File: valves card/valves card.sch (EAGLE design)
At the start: 68 parts, among them J1 TBP02R1-381-14BE, J2 09231486921, M1 SAM_D21_MINI_BREAKOUT, T1 IRLZ44NSTRLPBF, T10 IRLZ44NSTRLPBF, T11 IRLZ44NSTRLPBF, T12 IRLZ44NSTRLPBF, T2 IRLZ44NSTRLPBF, T3 IRLZ44NSTRLPBF, T4 IRLZ44NSTRLPBF, T5 IRLZ44NSTRLPBF, T6 IRLZ44NSTRLPBF, T7 IRLZ44NSTRLPBF, T8 IRLZ44NSTRLPBF, T9 IRLZ44NSTRLPBF, U1 LM2937IMP-12, U10 EL817(D)-ND, U11 EL817(D)-ND, U12 EL817(D)-ND, U13 EL817(D)-ND, U2 EL817(D)-ND, U3 EL817(D)-ND, U4 EL817(D)-ND, U5 EL817(D)-ND, U6 EL817(D)-ND, U7 EL817(D)-ND, U8 EL817(D)-ND, U9 EL817(D)-ND

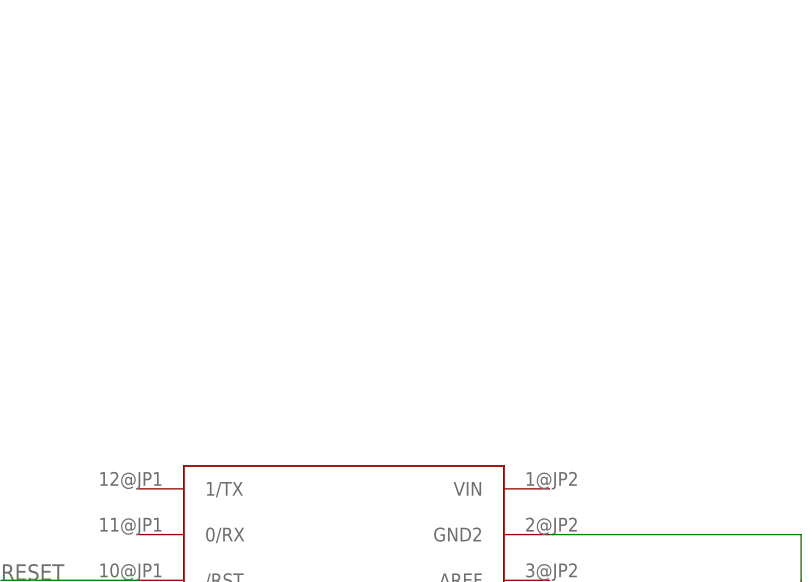
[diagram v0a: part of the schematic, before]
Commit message: made card holes bigger, started usb port work, but I'm not done that part yet
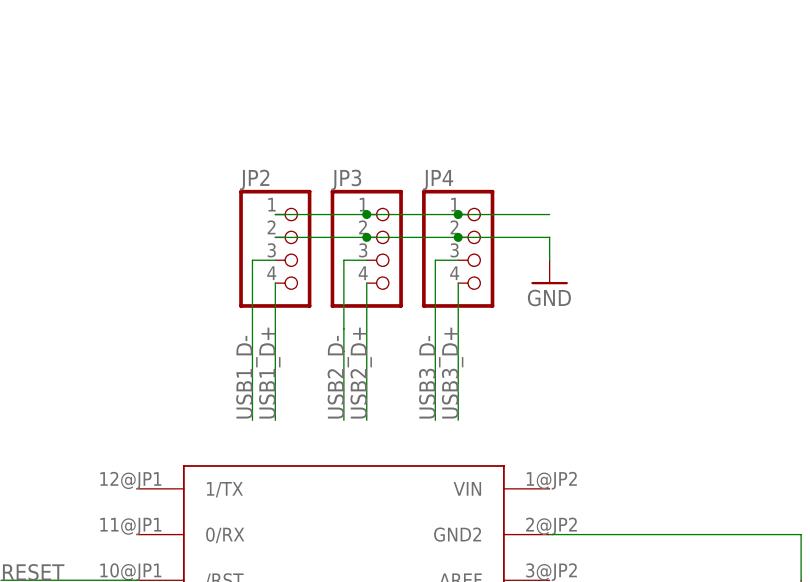
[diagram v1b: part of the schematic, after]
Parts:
- added JP2, JP3, JP4: (no value), pinhead:PINHD-1X4
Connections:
- net 5V: now also JP2.1, JP3.1, JP4.1
- net GND: now also JP2.2, JP3.2, JP4.2
- net USB1_D+: now also JP2.4
- net USB1_D-: now also JP2.3
- net USB2_D+: now also JP3.4
- net USB2_D-: now also JP3.3
- net USB3_D+: now also JP4.4
- net USB3_D-: now also JP4.3
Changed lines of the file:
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@@
 <part name="GND2" library="supply1" library_urn="urn:adsk.eagle:library:371" deviceset="GND" device=""/>
 <part name="GND3" library="supply1" library_urn="urn:adsk.eagle:library:371" deviceset="GND" device=""/>
+<part name="JP2" library="pinhead" library_urn="urn:adsk.eagle:library:325" deviceset="PINHD-1X4" device="" package3d_urn="urn:adsk.eagle:package:22407/2"/>
+<part name="JP3" library="pinhead" library_urn="urn:adsk.eagle:library:325" deviceset="PINHD-1X4" device="" package3d_urn="urn:adsk.eagle:package:22407/2"/>
+<part name="JP4" library="pinhead" library_urn="urn:adsk.eagle:library:325" deviceset="PINHD-1X4" device="" package3d_urn="urn:adsk.eagle:package:22407/2"/>
+<part name="GND7" library="supply1" library_urn="urn:adsk.eagle:library:371" deviceset="GND" device=""/>
 </parts>
 <sheets>
@@
 <attribute name="VALUE" x="-5.08" y="38.1" size="1.778" layer="96"/>
 </instance>
+<instance part="JP2" gate="A" x="71.12" y="93.98" smashed="yes">
+<attribute name="NAME" x="64.77" y="102.235" size="1.778" layer="95"/>
+<attribute name="VALUE" x="64.77" y="86.36" size="1.778" layer="96"/>
+</instance>
+<instance part="JP3" gate="A" x="81.28" y="93.98" smashed="yes">
+<attribute name="NAME" x="74.93" y="102.235" size="1.778" layer="95"/>
+<attribute name="VALUE" x="74.93" y="86.36" size="1.778" layer="96"/>
+</instance>
+<instance part="JP4" gate="A" x="91.44" y="93.98" smashed="yes">
+<attribute name="NAME" x="85.09" y="102.235" size="1.778" layer="95"/>
+<attribute name="VALUE" x="85.09" y="86.36" size="1.778" layer="96"/>
+</instance>
+<instance part="GND7" gate="1" x="99.06" y="91.44" smashed="yes">
+<attribute name="VALUE" x="96.52" y="88.9" size="1.778" layer="96"/>
+</instance>
 </instances>
 <busses>
@@
 <pinref part="J2" gate="G$1" pin="19"/>
 </segment>
+<segment>
+<pinref part="JP2" gate="A" pin="2"/>
+<pinref part="JP3" gate="A" pin="2"/>
+<wire x1="68.58" y1="96.52" x2="78.74" y2="96.52" width="0.1524" layer="91"/>
+<pinref part="JP4" gate="A" pin="2"/>
+<wire x1="78.74" y1="96.52" x2="88.9" y2="96.52" width="0.1524" layer="91"/>
+<junction x="78.74" y="96.52"/>
+<wire x1="88.9" y1="96.52" x2="99.06" y2="96.52" width="0.1524" layer="91"/>
+<junction x="88.9" y="96.52"/>
+<wire x1="99.06" y1="96.52" x2="99.06" y2="93.98" width="0.1524" layer="91"/>
+<pinref part="GND7" gate="1" pin="GND"/>
+</segment>
 </net>
 <net name="24V/12V" class="0">
@@
 <pinref part="J2" gate="G$1" pin="16"/>
 </segment>
+<segment>
+<pinref part="JP2" gate="A" pin="4"/>
+<wire x1="68.58" y1="91.44" x2="68.58" y2="76.2" width="0.1524" layer="91"/>
+<label x="68.58" y="76.2" size="1.778" layer="95" rot="R90"/>
+</segment>
 </net>
 <net name="CS_8" class="0">
@@
 <label x="0" y="48.26" size="1.778" layer="95"/>
 <pinref part="J2" gate="G$1" pin="32"/>
+</segment>
+<segment>
+<pinref part="JP3" gate="A" pin="4"/>
+<wire x1="78.74" y1="91.44" x2="78.74" y2="76.2" width="0.1524" layer="91"/>
+<label x="78.74" y="76.2" size="1.778" layer="95" rot="R90"/>
 </segment>
 </net>
@@
 <pinref part="J2" gate="G$1" pin="39"/>
 </segment>
+<segment>
+<pinref part="JP2" gate="A" pin="1"/>
+<pinref part="JP3" gate="A" pin="1"/>
+<wire x1="68.58" y1="99.06" x2="78.74" y2="99.06" width="0.1524" layer="91"/>
+<pinref part="JP4" gate="A" pin="1"/>
+<wire x1="78.74" y1="99.06" x2="88.9" y2="99.06" width="0.1524" layer="91"/>
+<junction x="78.74" y="99.06"/>
+<wire x1="88.9" y1="99.06" x2="99.06" y2="99.06" width="0.1524" layer="91"/>
+<junction x="88.9" y="99.06"/>
+</segment>
 </net>
 <net name="SDA" class="0">
@@
 <pinref part="J2" gate="G$1" pin="46"/>
 </segment>
+<segment>
+<pinref part="JP4" gate="A" pin="3"/>
+<wire x1="88.9" y1="93.98" x2="86.36" y2="93.98" width="0.1524" layer="91"/>
+<wire x1="86.36" y1="93.98" x2="86.36" y2="76.2" width="0.1524" layer="91"/>
+<label x="86.36" y="76.2" size="1.778" layer="95" rot="R90"/>
+</segment>
 </net>
 <net name="RESET" class="0">
@@
 <pinref part="J2" gate="G$1" pin="15"/>
 </segment>
+<segment>
+<pinref part="JP2" gate="A" pin="3"/>
+<wire x1="68.58" y1="93.98" x2="66.04" y2="93.98" width="0.1524" layer="91"/>
+<wire x1="66.04" y1="93.98" x2="66.04" y2="76.2" width="0.1524" layer="91"/>
+<label x="66.04" y="76.2" size="1.778" layer="95" rot="R90"/>
+</segment>
 </net>
 <net name="CS_6" class="0">
@@
 <pinref part="J2" gate="G$1" pin="31"/>
 </segment>
+<segment>
+<pinref part="JP3" gate="A" pin="3"/>
+<wire x1="78.74" y1="93.98" x2="76.2" y2="93.98" width="0.1524" layer="91"/>
+<wire x1="76.2" y1="93.98" x2="76.2" y2="86.36" width="0.1524" layer="91"/>
+<label x="76.2" y="76.2" size="1.778" layer="95" rot="R90"/>
+<wire x1="76.2" y1="86.36" x2="76.2" y2="83.82" width="0.1524" layer="91"/>
+<wire x1="76.2" y1="83.82" x2="76.2" y2="76.2" width="0.1524" layer="91"/>
+</segment>
 </net>
 <net name="CS_13" class="0">
@@
 <pinref part="J2" gate="G$1" pin="47"/>
 </segment>
-</net>
+<segment>
+<pinref part="JP4" gate="A" pin="4"/>
+<wire x1="88.9" y1="91.44" x2="88.9" y2="76.2" width="0.1524" layer="91"/>
+<label x="88.9" y="76.2" size="1.778" layer="95" rot="R90"/>
+</segment>
+</net>

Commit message: USB system mods complete on the main board, valves board, and motor board
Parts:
- renumbered M1 to M2
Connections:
- new net N$1: M2.GND
- net GND: no longer M2.GND
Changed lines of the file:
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@@
 <part name="GND13" library="supply1" library_urn="urn:adsk.eagle:library:371" deviceset="GND" device=""/>
 <part name="GND14" library="supply1" library_urn="urn:adsk.eagle:library:371" deviceset="GND" device=""/>
-<part name="M1" library="SparkFun-SAMD21-Mini-Breakout" deviceset="SAM_D21_MINI_BREAKOUT" device=""/>
 <part name="T1" library="BUK9214-30A,118" deviceset="BUK9214-30A-118" device="-DPAK" package3d_urn="urn:adsk.eagle:package:30824558/1" value="IRLZ44NSTRLPBF"/>
 <part name="J1" library="TBP02R1-381-14BE" deviceset="TBP02R1-381-14BE" device=""/>
@@
 <part name="JP4" library="pinhead" library_urn="urn:adsk.eagle:library:325" deviceset="PINHD-1X4" device="" package3d_urn="urn:adsk.eagle:package:22407/2"/>
 <part name="GND7" library="supply1" library_urn="urn:adsk.eagle:library:371" deviceset="GND" device=""/>
+<part name="M2" library="SparkFun-SAMD21-Mini-Breakout" deviceset="SAM_D21_MINI_BREAKOUT" device=""/>
 </parts>
 <sheets>
@@
 <attribute name="VALUE" x="259.08" y="-20.32" size="1.778" layer="96"/>
 </instance>
-<instance part="M1" gate="G$1" x="76.2" y="35.56" smashed="yes"/>
 <instance part="T1" gate="T" x="254" y="55.88" smashed="yes">
 <attribute name="NAME" x="251.46" y="56.642" size="1.778" layer="95" rot="R90"/>
@@
 <attribute name="VALUE" x="96.52" y="88.9" size="1.778" layer="96"/>
 </instance>
+<instance part="M2" gate="G$1" x="76.2" y="35.56" smashed="yes"/>
 </instances>
 <busses>
@@
 </segment>
 <segment>
-<pinref part="M1" gate="G$1" pin="GND2"/>
 <wire x1="99.06" y1="63.5" x2="127" y2="63.5" width="0.1524" layer="91"/>
 <wire x1="127" y1="63.5" x2="127" y2="58.42" width="0.1524" layer="91"/>
 <pinref part="GND4" gate="1" pin="GND"/>
-</segment>
-<segment>
-<pinref part="M1" gate="G$1" pin="GND"/>
-<wire x1="53.34" y1="53.34" x2="35.56" y2="53.34" width="0.1524" layer="91"/>
-<wire x1="35.56" y1="53.34" x2="35.56" y2="50.8" width="0.1524" layer="91"/>
-<pinref part="GND5" gate="1" pin="GND"/>
+<pinref part="M2" gate="G$1" pin="GND2"/>
 </segment>
 <segment>
@@
 <net name="3.3V" class="0">
 <segment>
-<pinref part="M1" gate="G$1" pin="VCC"/>
 <wire x1="99.06" y1="53.34" x2="121.92" y2="53.34" width="0.1524" layer="91"/>
 <label x="109.22" y="53.34" size="1.778" layer="95"/>
+<pinref part="M2" gate="G$1" pin="VCC"/>
 </segment>
 <segment>
@@
 <net name="SCK" class="0">
 <segment>
-<pinref part="M1" gate="G$1" pin="13"/>
 <wire x1="99.06" y1="27.94" x2="121.92" y2="27.94" width="0.1524" layer="91"/>
 <label x="109.22" y="27.94" size="1.778" layer="95"/>
+<pinref part="M2" gate="G$1" pin="13"/>
 </segment>
 <segment>
@@
 <net name="MISO" class="0">
 <segment>
-<pinref part="M1" gate="G$1" pin="12"/>
 <wire x1="99.06" y1="22.86" x2="121.92" y2="22.86" width="0.1524" layer="91"/>
 <label x="109.22" y="22.86" size="1.778" layer="95"/>
+<pinref part="M2" gate="G$1" pin="12"/>
 </segment>
 <segment>
@@
 <net name="MOSI" class="0">
 <segment>
-<pinref part="M1" gate="G$1" pin="11"/>
 <wire x1="99.06" y1="17.78" x2="121.92" y2="17.78" width="0.1524" layer="91"/>
 <label x="109.22" y="17.78" size="1.778" layer="95"/>
+<pinref part="M2" gate="G$1" pin="11"/>
 </segment>
 <segment>
@@
 </segment>
 <segment>
-<pinref part="M1" gate="G$1" pin="2"/>
 <wire x1="53.34" y1="48.26" x2="40.64" y2="48.26" width="0.1524" layer="91"/>
 <label x="40.64" y="48.26" size="1.778" layer="95"/>
+<pinref part="M2" gate="G$1" pin="2"/>
 </segment>
 </net>
@@
 </segment>
 <segment>
-<pinref part="M1" gate="G$1" pin="3"/>
 <wire x1="53.34" y1="43.18" x2="40.64" y2="43.18" width="0.1524" layer="91"/>
 <label x="40.64" y="43.18" size="1.778" layer="95"/>
+<pinref part="M2" gate="G$1" pin="3"/>
 </segment>
 </net>
@@
 </segment>
 <segment>
-<pinref part="M1" gate="G$1" pin="4"/>
 <wire x1="53.34" y1="38.1" x2="40.64" y2="38.1" width="0.1524" layer="91"/>
 <label x="40.64" y="38.1" size="1.778" layer="95"/>
+<pinref part="M2" gate="G$1" pin="4"/>
 </segment>
 </net>
@@
 </segment>
 <segment>
-<pinref part="M1" gate="G$1" pin="5"/>
 <wire x1="53.34" y1="33.02" x2="40.64" y2="33.02" width="0.1524" layer="91"/>
 <label x="40.64" y="33.02" size="1.778" layer="95"/>
+<pinref part="M2" gate="G$1" pin="5"/>
 </segment>
 </net>
@@
 </segment>
 <segment>
-<pinref part="M1" gate="G$1" pin="6"/>
 <wire x1="53.34" y1="27.94" x2="40.64" y2="27.94" width="0.1524" layer="91"/>
 <label x="40.64" y="27.94" size="1.778" layer="95"/>
+<pinref part="M2" gate="G$1" pin="6"/>
 </segment>
 </net>
@@
 </segment>
 <segment>
-<pinref part="M1" gate="G$1" pin="7"/>
 <wire x1="53.34" y1="22.86" x2="38.1" y2="22.86" width="0.1524" layer="91"/>
 <label x="40.64" y="22.86" size="1.778" layer="95"/>
+<pinref part="M2" gate="G$1" pin="7"/>
 </segment>
 </net>
@@
 </segment>
 <segment>
-<pinref part="M1" gate="G$1" pin="8"/>
 <wire x1="53.34" y1="17.78" x2="38.1" y2="17.78" width="0.1524" layer="91"/>
 <label x="40.64" y="17.78" size="1.778" layer="95"/>
+<pinref part="M2" gate="G$1" pin="8"/>
 </segment>
 </net>
@@
 </segment>
 <segment>
-<pinref part="M1" gate="G$1" pin="9"/>
 <wire x1="53.34" y1="12.7" x2="38.1" y2="12.7" width="0.1524" layer="91"/>
 <label x="40.64" y="12.7" size="1.778" layer="95"/>
+<pinref part="M2" gate="G$1" pin="9"/>
 </segment>
 </net>
@@
 </segment>
 <segment>
-<pinref part="M1" gate="G$1" pin="A0"/>
 <wire x1="99.06" y1="33.02" x2="121.92" y2="33.02" width="0.1524" layer="91"/>
 <label x="109.22" y="33.02" size="1.778" layer="95"/>
+<pinref part="M2" gate="G$1" pin="A0"/>
 </segment>
 </net>
@@
 </segment>
 <segment>
-<pinref part="M1" gate="G$1" pin="A1"/>
 <wire x1="121.92" y1="38.1" x2="99.06" y2="38.1" width="0.1524" layer="91"/>
 <label x="109.22" y="38.1" size="1.778" layer="95"/>
+<pinref part="M2" gate="G$1" pin="A1"/>
 </segment>
 </net>
@@
 </segment>
 <segment>
-<pinref part="M1" gate="G$1" pin="A2"/>
 <wire x1="99.06" y1="43.18" x2="121.92" y2="43.18" width="0.1524" layer="91"/>
 <label x="109.22" y="43.18" size="1.778" layer="95"/>
+<pinref part="M2" gate="G$1" pin="A2"/>
 </segment>
 </net>
@@
 </segment>
 <segment>
-<pinref part="M1" gate="G$1" pin="A3"/>
 <wire x1="121.92" y1="48.26" x2="99.06" y2="48.26" width="0.1524" layer="91"/>
 <label x="109.22" y="48.26" size="1.778" layer="95"/>
+<pinref part="M2" gate="G$1" pin="A3"/>
 </segment>
 </net>
@@
 <segment>
 <pinref part="SJ1" gate="1" pin="1"/>
-<pinref part="M1" gate="G$1" pin="10"/>
 <wire x1="132.08" y1="12.7" x2="129.54" y2="12.7" width="0.1524" layer="91"/>
 <pinref part="JP1" gate="G$1" pin="1"/>
@@
 <wire x1="129.54" y1="20.32" x2="129.54" y2="12.7" width="0.1524" layer="91"/>
 <junction x="129.54" y="12.7"/>
+<pinref part="M2" gate="G$1" pin="10"/>
 </segment>
 </net>
@@
 </segment>
 <segment>
-<pinref part="M1" gate="G$1" pin="/RST"/>
 <wire x1="53.34" y1="58.42" x2="38.1" y2="58.42" width="0.1524" layer="91"/>
 <label x="38.1" y="58.42" size="1.778" layer="95"/>
+<pinref part="M2" gate="G$1" pin="/RST"/>
 </segment>
 </net>
@@
 </segment>
 </net>
+<net name="N$1" class="0">
+<segment>
+<wire x1="53.34" y1="53.34" x2="35.56" y2="53.34" width="0.1524" layer="91"/>
+<wire x1="35.56" y1="53.34" x2="35.56" y2="50.8" width="0.1524" layer="91"/>
+<pinref part="GND5" gate="1" pin="GND"/>
+<pinref part="M2" gate="G$1" pin="GND"/>
+</segment>
+</net>

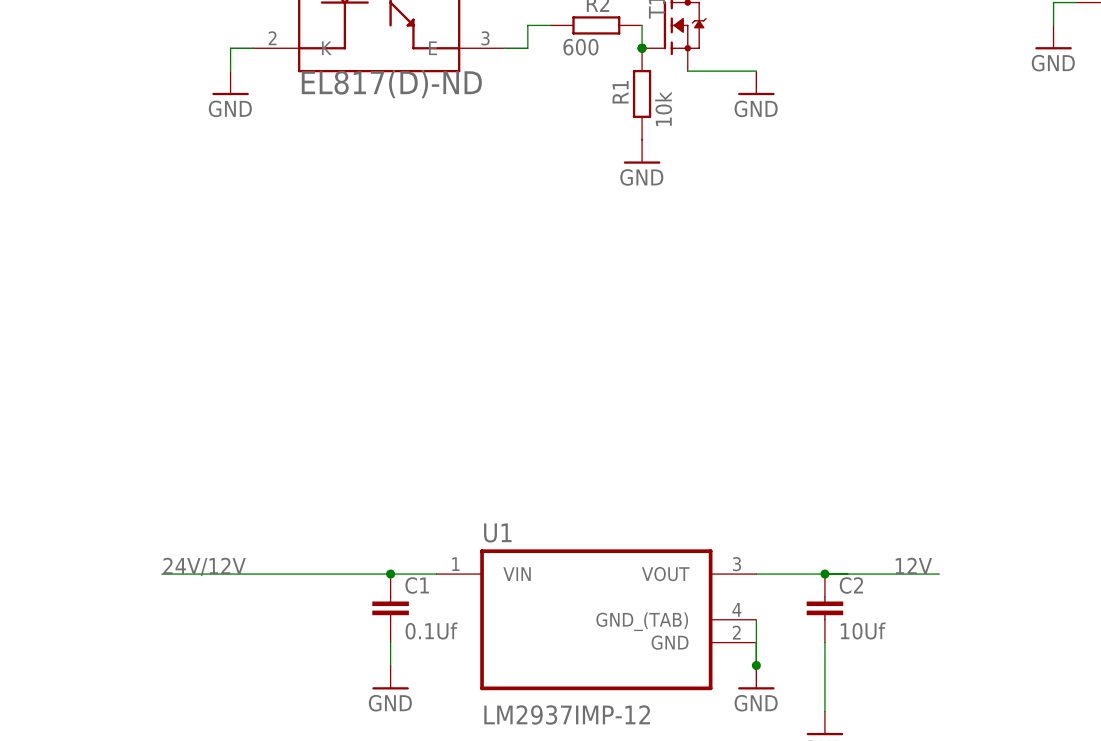
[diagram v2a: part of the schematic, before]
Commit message: added on light to main card
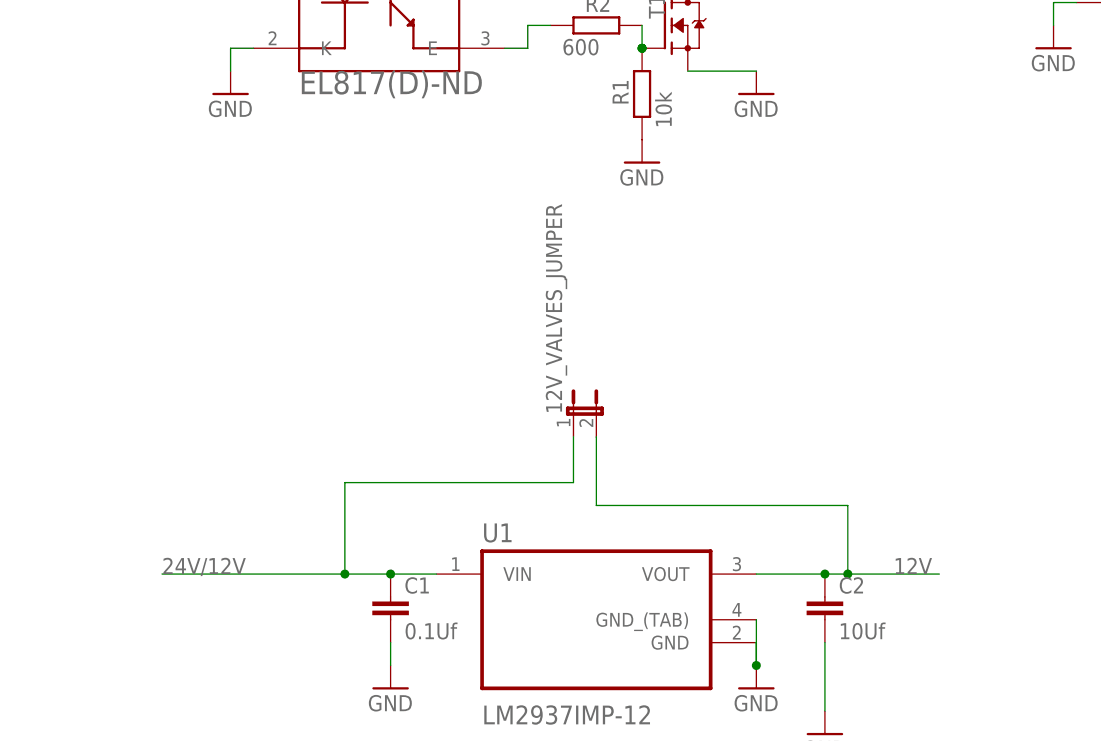
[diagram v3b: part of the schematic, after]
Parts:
- added 12V_VALVES_JUMPER: (no value), SparkFun-Passives:JUMPER-2SMD-NO
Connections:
- net 12V: now also 12V_VALVES_JUMPER.2
- net 24V/12V: now also 12V_VALVES_JUMPER.1
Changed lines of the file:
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@@
 <part name="GND7" library="supply1" library_urn="urn:adsk.eagle:library:371" deviceset="GND" device=""/>
 <part name="M2" library="SparkFun-SAMD21-Mini-Breakout" deviceset="SAM_D21_MINI_BREAKOUT" device=""/>
+<part name="12V_VALVES_JUMPER" library="SparkFun-Passives" deviceset="JUMPER-2" device="SMD-NO" package3d_urn="urn:adsk.eagle:package:30824506/1"/>
 </parts>
 <sheets>
@@
 </instance>
 <instance part="M2" gate="G$1" x="76.2" y="35.56" smashed="yes"/>
+<instance part="12V_VALVES_JUMPER" gate="A" x="241.3" y="12.7" smashed="yes">
+<attribute name="NAME" x="240.03" y="12.7" size="1.778" layer="95" rot="R90"/>
+<attribute name="VALUE" x="247.015" y="12.7" size="1.778" layer="96" rot="R90"/>
+</instance>
 </instances>
 <busses>
@@
 <pinref part="C1" gate="G$1" pin="1"/>
 <wire x1="226.06" y1="-5.08" x2="220.98" y2="-5.08" width="0.1524" layer="91"/>
-<wire x1="220.98" y1="-5.08" x2="195.58" y2="-5.08" width="0.1524" layer="91"/>
+<wire x1="220.98" y1="-5.08" x2="215.9" y2="-5.08" width="0.1524" layer="91"/>
 <junction x="220.98" y="-5.08"/>
 <label x="195.58" y="-5.08" size="1.778" layer="95"/>
+<wire x1="215.9" y1="-5.08" x2="195.58" y2="-5.08" width="0.1524" layer="91"/>
+<wire x1="215.9" y1="-5.08" x2="215.9" y2="5.08" width="0.1524" layer="91"/>
+<junction x="215.9" y="-5.08"/>
+<wire x1="215.9" y1="5.08" x2="241.3" y2="5.08" width="0.1524" layer="91"/>
+<wire x1="241.3" y1="5.08" x2="241.3" y2="10.16" width="0.1524" layer="91"/>
+<pinref part="12V_VALVES_JUMPER" gate="A" pin="1"/>
 </segment>
 <segment>
@@
 <pinref part="C2" gate="G$1" pin="1"/>
 <wire x1="261.62" y1="-5.08" x2="269.24" y2="-5.08" width="0.1524" layer="91"/>
-<wire x1="271.78" y1="-5.08" x2="269.24" y2="-5.08" width="0.1524" layer="91"/>
 <junction x="269.24" y="-5.08"/>
-<wire x1="269.24" y1="-5.08" x2="281.94" y2="-5.08" width="0.1524" layer="91"/>
+<wire x1="269.24" y1="-5.08" x2="271.78" y2="-5.08" width="0.1524" layer="91"/>
 <label x="276.86" y="-5.08" size="1.778" layer="95"/>
-</segment>
-<segment>
+<wire x1="271.78" y1="-5.08" x2="281.94" y2="-5.08" width="0.1524" layer="91"/>
+<wire x1="243.84" y1="10.16" x2="243.84" y2="2.54" width="0.1524" layer="91"/>
+<wire x1="243.84" y1="2.54" x2="271.78" y2="2.54" width="0.1524" layer="91"/>
+<wire x1="271.78" y1="2.54" x2="271.78" y2="-5.08" width="0.1524" layer="91"/>
+<junction x="271.78" y="-5.08"/>
+<pinref part="12V_VALVES_JUMPER" gate="A" pin="2"/>
+</segment>
+<segment>

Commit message: final mods to the boards, next commit will add the CAM data, it will be the final commit before the polyvent V2.1 design merge, and I'm ready to order boards
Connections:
- removed net N$1: M2.GND
- net GND: now also M2.GND
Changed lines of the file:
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@@
 <pinref part="GND7" gate="1" pin="GND"/>
+</segment>
+<segment>
+<wire x1="35.56" y1="53.34" x2="35.56" y2="50.8" width="0.1524" layer="91"/>
+<pinref part="GND5" gate="1" pin="GND"/>
+<pinref part="M2" gate="G$1" pin="GND"/>
+<wire x1="53.34" y1="53.34" x2="35.56" y2="53.34" width="0.1524" layer="91"/>
 </segment>
 </net>
@@
 </segment>
 </net>
-<net name="N$1" class="0">
-<segment>
-<wire x1="53.34" y1="53.34" x2="35.56" y2="53.34" width="0.1524" layer="91"/>
-<wire x1="35.56" y1="53.34" x2="35.56" y2="50.8" width="0.1524" layer="91"/>
-<pinref part="GND5" gate="1" pin="GND"/>
-<pinref part="M2" gate="G$1" pin="GND"/>
-</segment>
-</net>

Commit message: updated libraries to generate better bom's
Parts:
- C1: value 0.1Uf -> 0.1Uf, 50V; device eagle-ltspice:C -> SparkFun-Passives:CAP0805
- C2: value 10Uf -> 10Uf, 50V; device eagle-ltspice:CC1206 -> SparkFun-Passives:CAP0805
- R1, R10, R11, R12, R13, R14, R15, R16, R17, R18, R19, R2, R20, R21, R22, R23, R24, R25, R26, R27, R28, R29, R3, R30, R31, R32, R33, R34, R35, R36, R4, R5, R6, R7, R8, R9: device eagle-ltspice:R -> SparkFun-Passives:RESISTOR0805-RES
- U1: device LM2937IMP-10:LM2937IMP-10 -> LM2937IMP-10:LM2937IMP-12
- U10, U11, U12, U13, U4, U5, U6, U7, U8, U9: device EL817C:EL817C -> EL817(D):EL817(D)
- U2: device EL817C:EL817C -> EL817(D):EL817(D); BEST_I_COULD_FIND EL817(D)-ND -> (none); MP OR-815 -> (none)
- U3: device EL817C:EL817C -> EL817(D):EL817(D); MP OR-815 -> (none)
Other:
- note added: "Connectors"
- note added: "Microcontroller"
- note added: "Mosfet channels"
- note added: "Power supply for MOSFET Gates"
- moved on the sheet: 12V_VALVES_JUMPER, C1, C2, J1, J2, JP1, JP2, JP3, JP4, SJ1, U1
